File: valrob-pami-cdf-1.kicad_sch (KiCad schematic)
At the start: 106 parts, among them J1 Conn_01x04, J10 Conn_01x04_Pin, J3 USB_C_Receptacle_USB2.0_14P, J4 Conn_01x02, M1 Motor_Servo, Q1 Q_NMOS, Q2 Q_NMOS, Q3 Q_NMOS, SW1 SW_SPST, SW3 SW_Push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

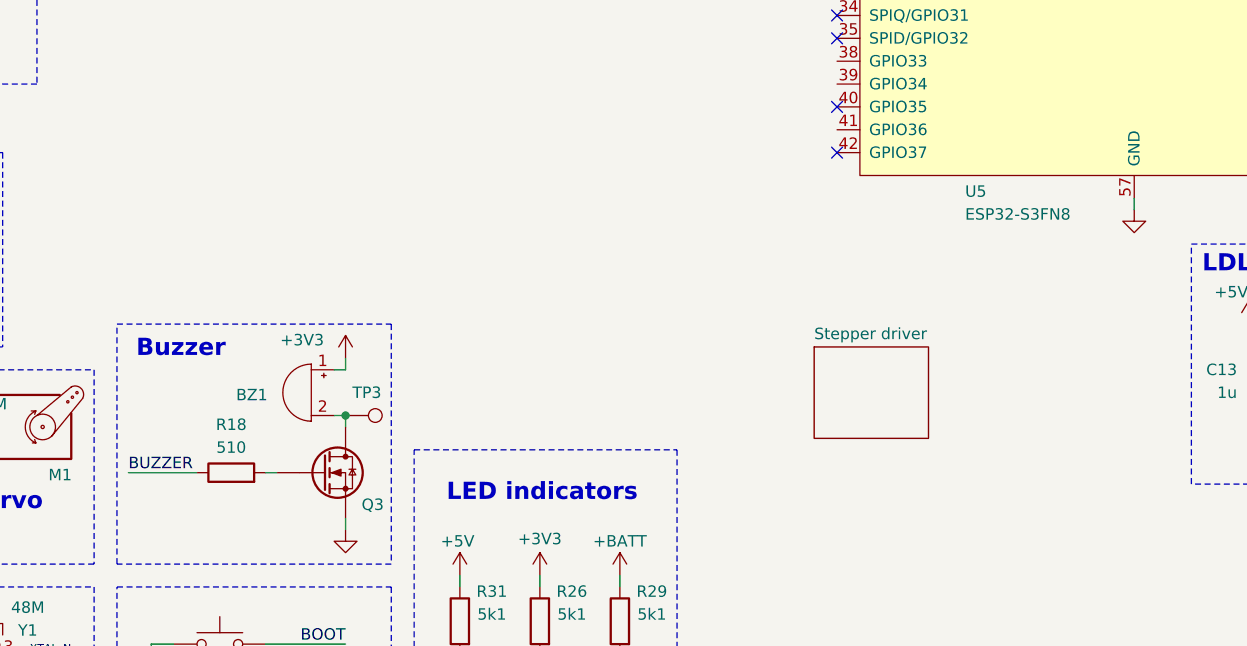
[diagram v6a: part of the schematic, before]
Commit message: schem: import BATT sense from valrob-alim
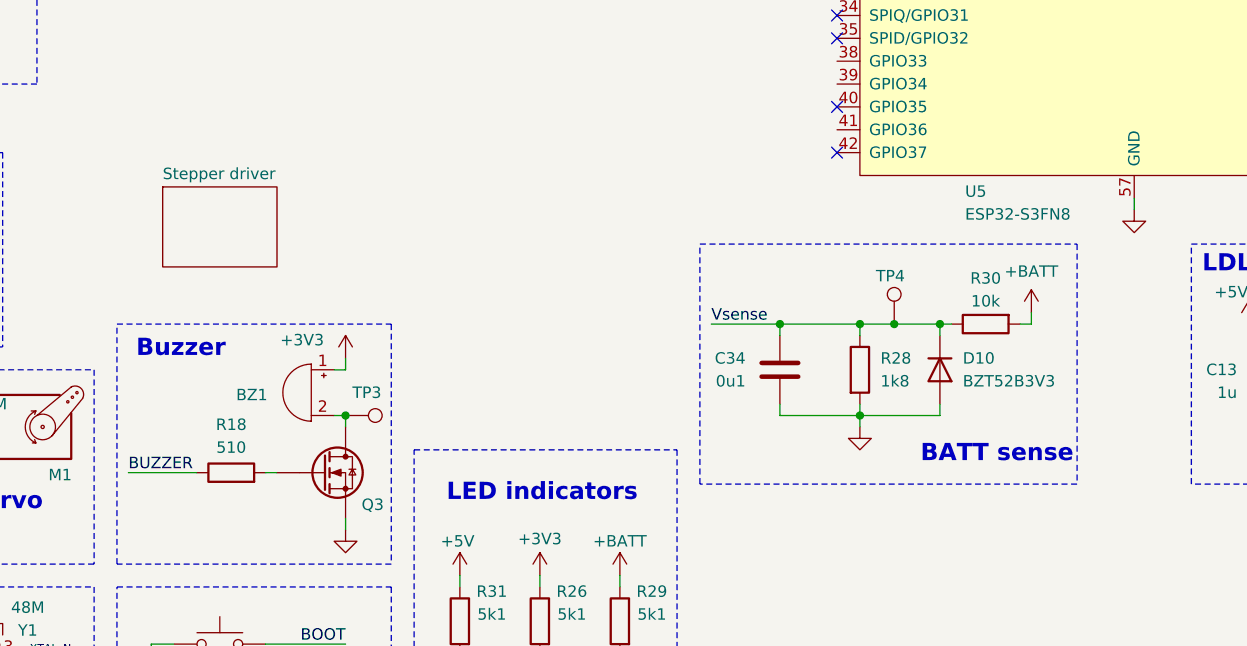
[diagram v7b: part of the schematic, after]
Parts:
- added C34: 0u1, Capacitor_SMD:C_0402_1005Metric, symbol Device:C
- added D10: BZT52B3V3, Diode_SMD:D_SOD-123, symbol Device:D
- added R28: 1k8, Resistor_SMD:R_0603_1608Metric, symbol Device:R
- added R30: 10k, Resistor_SMD:R_0402_1005Metric, symbol Device:R
- added TP4: TestPoint, TestPoint:TestPoint_Pad_D2.0mm, symbol Connector:TestPoint
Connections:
- net +BATT: now also R30.2
- net GND: now also C34.2, D10.2 (A), R28.2
- new net Vsense: C34.1, D10.1 (K), R28.1, R30.1, TP4.1
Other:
- note added: "BATT sense"

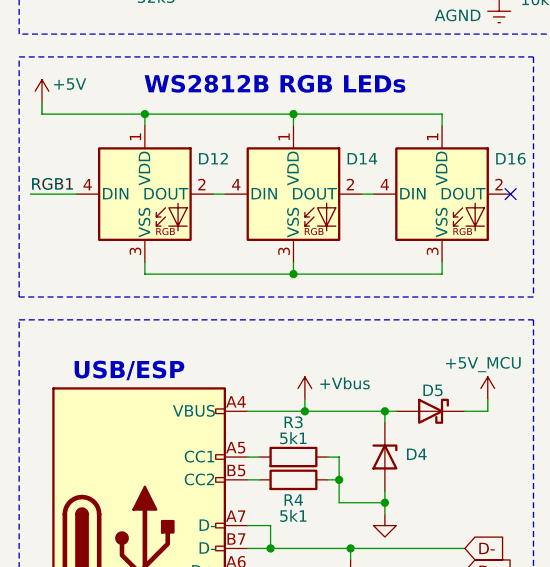
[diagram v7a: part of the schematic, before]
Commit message: schem: add missing rgb leds ground symbol
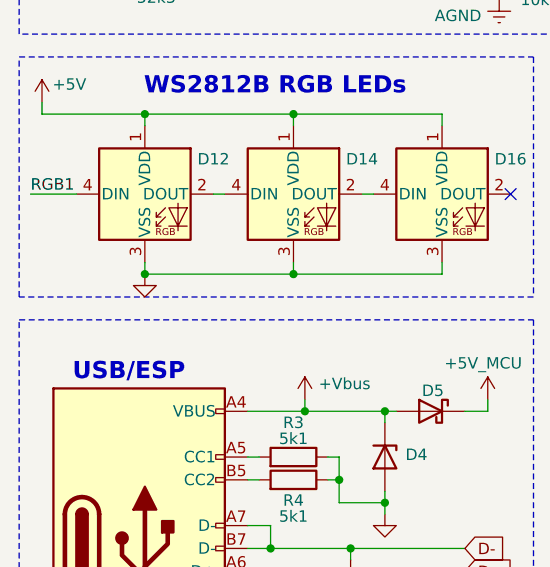
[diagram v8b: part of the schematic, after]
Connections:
- net GND: now also D12.3 (VSS), D14.3 (VSS), D16.3 (VSS)
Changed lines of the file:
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@@
 	)
 	(junction
+		(at 27.94 146.05)
+		(diameter 0)
+		(color 0 0 0 0)
+	)
+	(junction
 		(at 50.8 176.53)
 		(diameter 0)
@@
 					(unit 1)
 				)
+			)
+		)
+	)
+	(symbol
+		(lib_id "power:GND")
+		(at 27.94 146.05 0)
+		(unit 1)
+		(exclude_from_sim no)
+		(in_bom yes)
+		(on_board yes)
+		(dnp no)
+		(property "Reference" "#PWR058"
+			(at 27.94 152.4 0)
+			(effects
+				(font
+					(size 1.27 1.27)
+				)
+				(hide yes)
+			)
+		)
+		(property "Value" "GND"
+			(at 27.94 150.368 0)
+			(effects
+				(font
+					(size 1.27 1.27)
+				)
+				(hide yes)
+			)
+		)
+		(property "Footprint" ""
+			(at 27.94 146.05 0)
+			(effects
+				(font
+					(size 1.27 1.27)
+				)
+				(hide yes)
+			)
+		)
+		(property "Datasheet" ""
+			(at 27.94 146.05 0)
+			(effects
+				(font
+					(size 1.27 1.27)
+				)
+				(hide yes)
+			)
+		)
+		(property "Description" "Power symbol creates a global label with name \"GND\" , ground"
+			(at 27.94 146.05 0)
+			(effects
+				(font
+					(size 1.27 1.27)
+				)
+				(hide yes)
+			)
+		)
+		(pin "1"
+		)
+		(instances
+			(project "valrob-pami-cdf-1"
+				(path "/453def7e-2a78-4c3c-a4b7-f12883e5bdd2"
+					(reference "#PWR058")
+					(unit 1)
+				)
